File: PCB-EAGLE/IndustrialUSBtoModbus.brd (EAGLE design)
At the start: 65 x 26.6 mm, 51 parts, among them IC10 ADUM1201ARZ, IC11 ADUM1201ARZ, IC2 MAX485CSA+, IC4 FT231XS-R

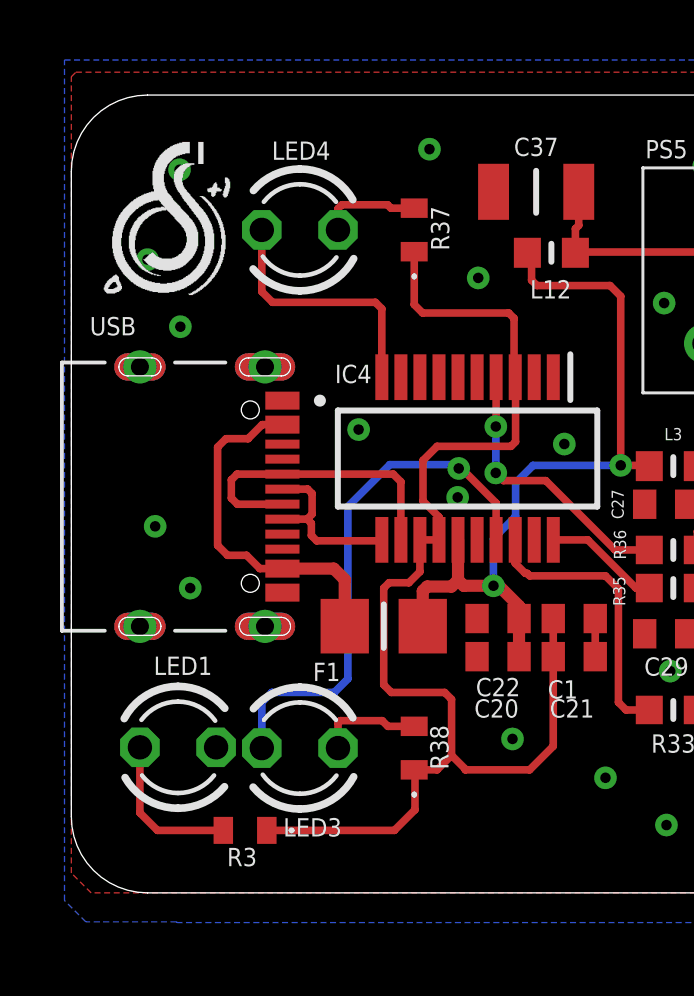
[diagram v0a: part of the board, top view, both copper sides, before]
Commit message: docs: add buyer-ready project documentation
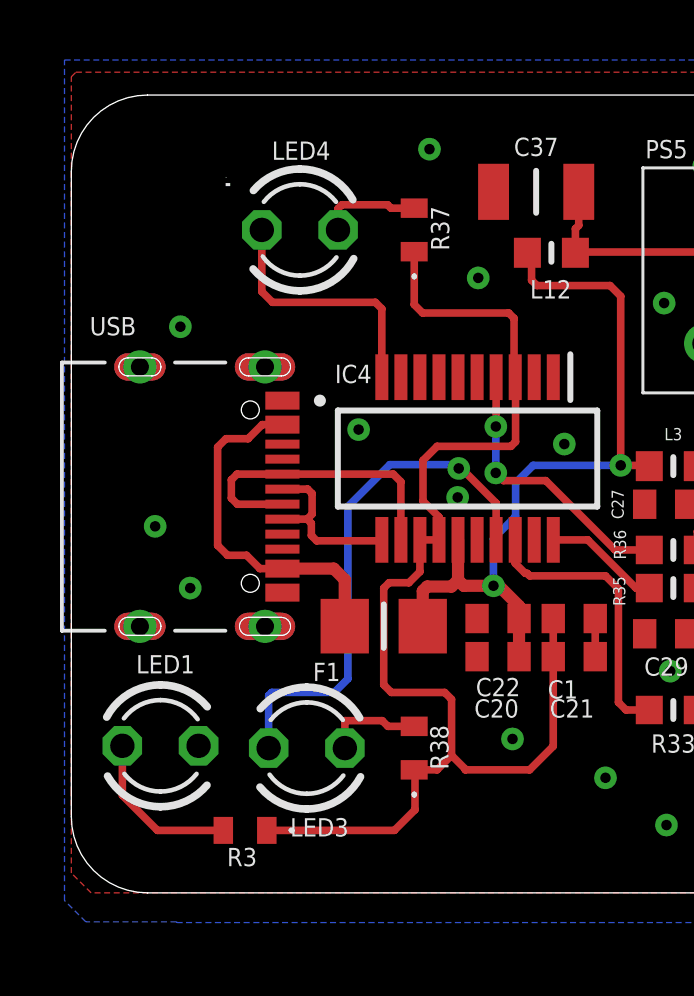
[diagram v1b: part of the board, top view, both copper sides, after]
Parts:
- moved LED1 0.59 mm to (3.23, 61.8)
- moved LED3 0.23 mm to (8.10, 61.7)
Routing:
- net GND: vias 16 -> 14
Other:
- board text removed: "Industrial USB to MODBUS By POSITRON ELECTRONIC"

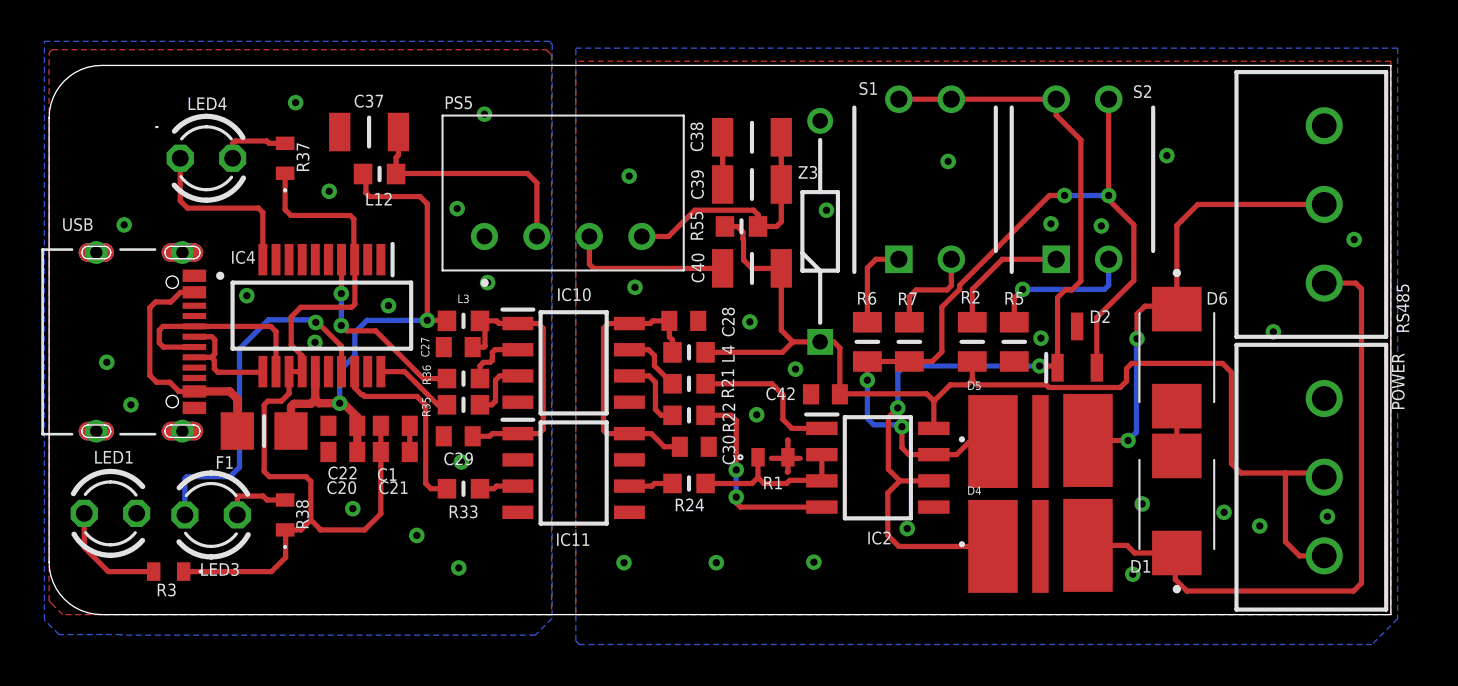
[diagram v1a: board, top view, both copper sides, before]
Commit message: feat: update USB RS485 hardware revision
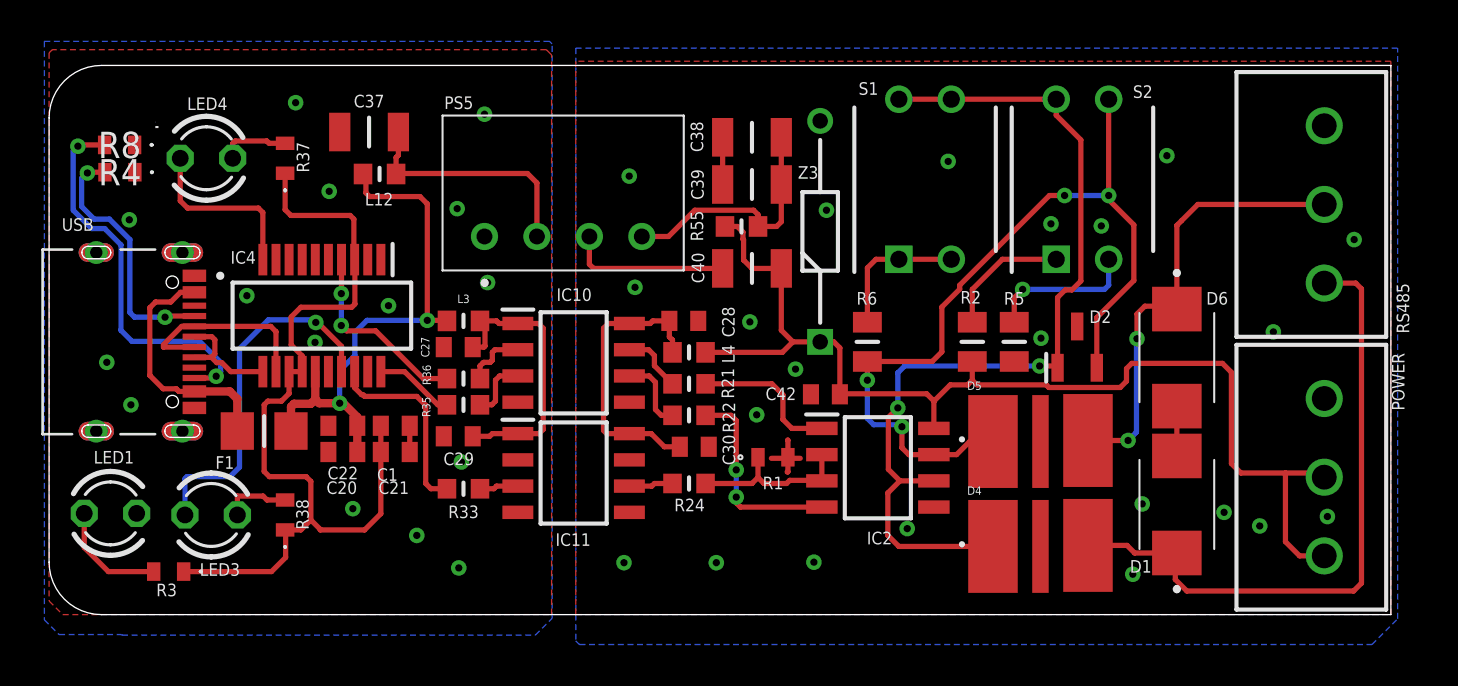
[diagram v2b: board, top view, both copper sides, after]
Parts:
- removed R7: 120, SamacSys_Parts:RESC2012X65N
- added R4, R8: 5.1k, AKCP:ERJH3
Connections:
- removed net N$16: R7.2, S1.2
- new net CC1: R4.2, USB.A5
- new net CC2: R8.2, USB.B5
- net B: no longer R7.1
- net GND: now also R4.1, R8.1
- net N$15: now also S1.2
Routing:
- net CC2: track 0.00 -> 19.0 mm, vias 0 -> 2
- net CC1: track 0.00 -> 12.4 mm, vias 0 -> 2
- net N$16: track 4.77 -> 0.00 mm
- net N$15: track 4.33 -> 6.87 mm
- net D-: track 10.2 -> 9.48 mm
